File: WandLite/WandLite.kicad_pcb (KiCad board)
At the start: 2 copper layers, 11.7 x 25 mm, 6 parts, among them U1 ATtiny85-20P

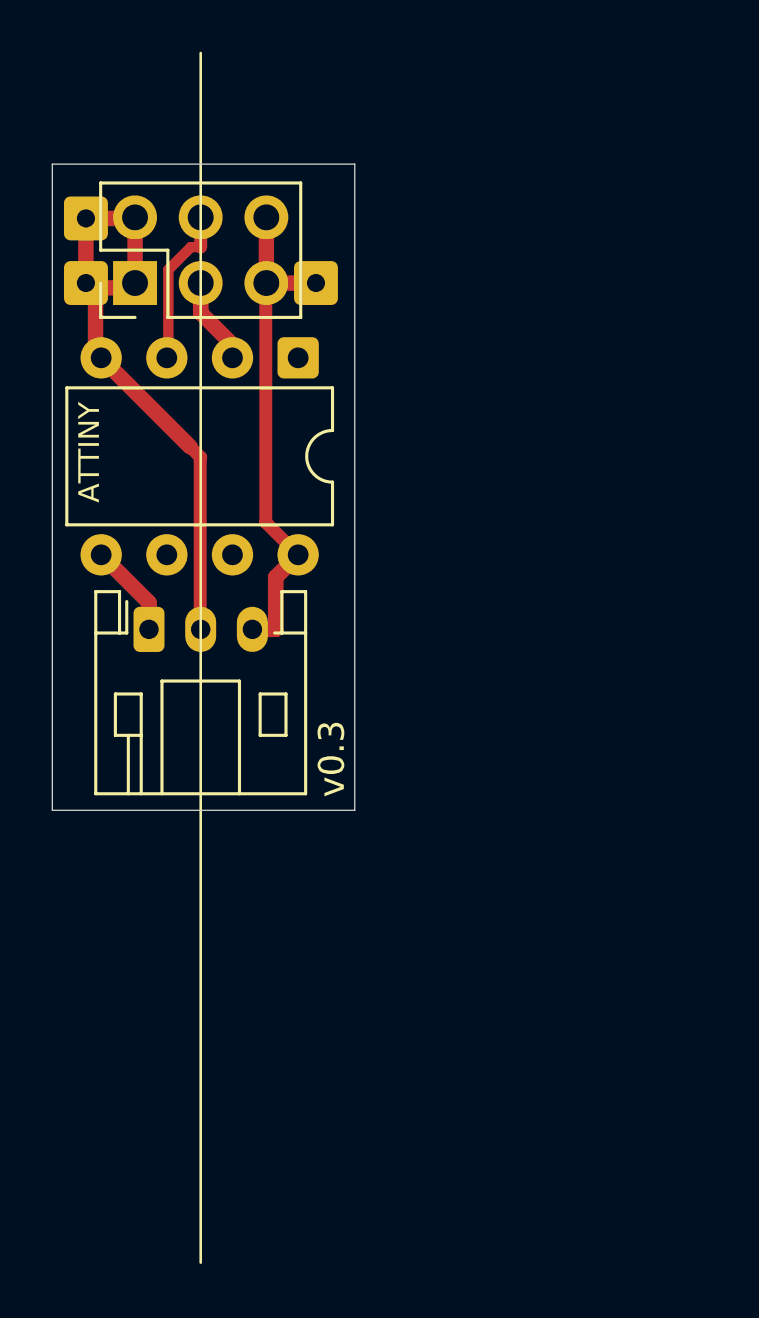
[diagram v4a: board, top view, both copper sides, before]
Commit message: flipped board to BU
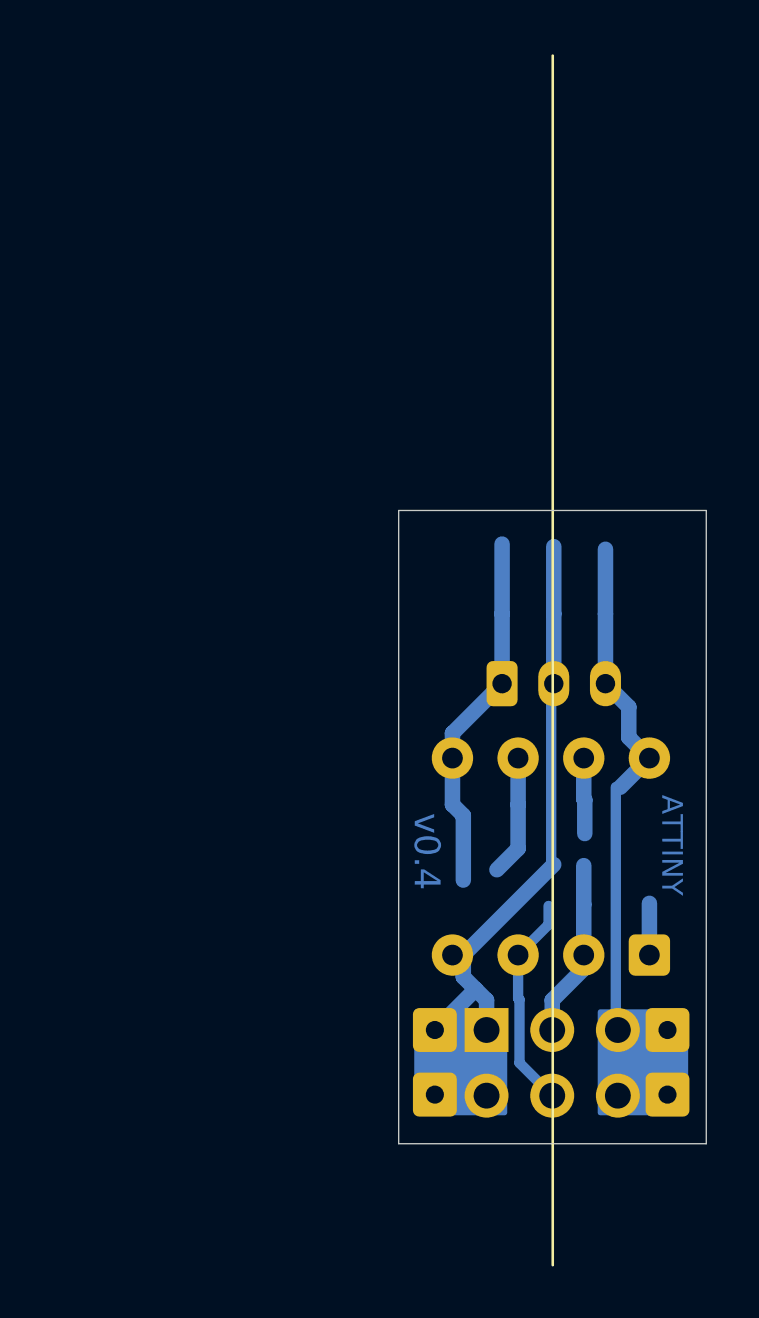
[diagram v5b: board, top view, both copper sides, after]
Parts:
- added ?: , , F.Cu at (170.6, 131.4)
- BLD-O1, GND-I1, GND-I2, J-IN1, U1, VCC-I1: moved to B.Cu
- moved GND-I1 36.5 mm to (161.6, 131.4)
- moved J-IN1 31.9 mm to (163.6, 128.9), turned to -90 degrees
- moved VCC-I1 31.9 mm to (170.6, 128.9)
- moved GND-I2 31.9 mm to (161.6, 128.9)
- moved U1 26.8 mm to (169.9, 126.0), turned to 90 degrees
- moved BLD-O1 13.8 mm to (164.2, 115.5)
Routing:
- net Net-(BLD-O1-Pin_1): track 3.65 -> 14.0 mm
- net VCC: track 19.6 -> 28.7 mm
- net GND: track 24.5 -> 32.3 mm
- net unconnected-(U1-PB1-Pad6): track 0.00 -> 4.66 mm
- net Net-(J-IN1-Pin_3): track 3.40 -> 6.98 mm
- net unconnected-(U1-PB2-Pad7): track 0.00 -> 2.94 mm
- net Net-(J-IN1-Pin_4): track 6.20 -> 8.38 mm
- net unconnected-(U1-~{RESET}/PB5-Pad1): track 0.00 -> 2.00 mm
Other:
- board size 11.7 x 25 mm -> 11.9 x 24.5 mm
- board text added: "v0.4"
- board text removed: "v0.3"
